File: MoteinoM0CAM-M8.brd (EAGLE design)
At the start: 22.6 x 22.2 mm, 17 parts

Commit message: doco update
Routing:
- net GND: vias 11 -> 12
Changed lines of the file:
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@@
 <via x="3.302" y="14.986" extent="1-16" drill="0.35"/>
 <via x="4.445" y="19.304" extent="1-16" drill="0.35"/>
+<via x="18.542" y="18.796" extent="1-16" drill="0.35"/>
+<wire x1="18.669" y1="16.129" x2="18.542" y2="18.796" width="0" layer="19" extent="1-1"/>
 </signal>
 <signal name="SDA">
@@
 <wire x1="7.112" y1="0" x2="7.088" y2="0" width="0.1524" layer="1"/>
 </signal>
-<signal name="N$13">
-<via x="18.542" y="18.796" extent="1-16" drill="0.35"/>
-</signal>
 </signals>

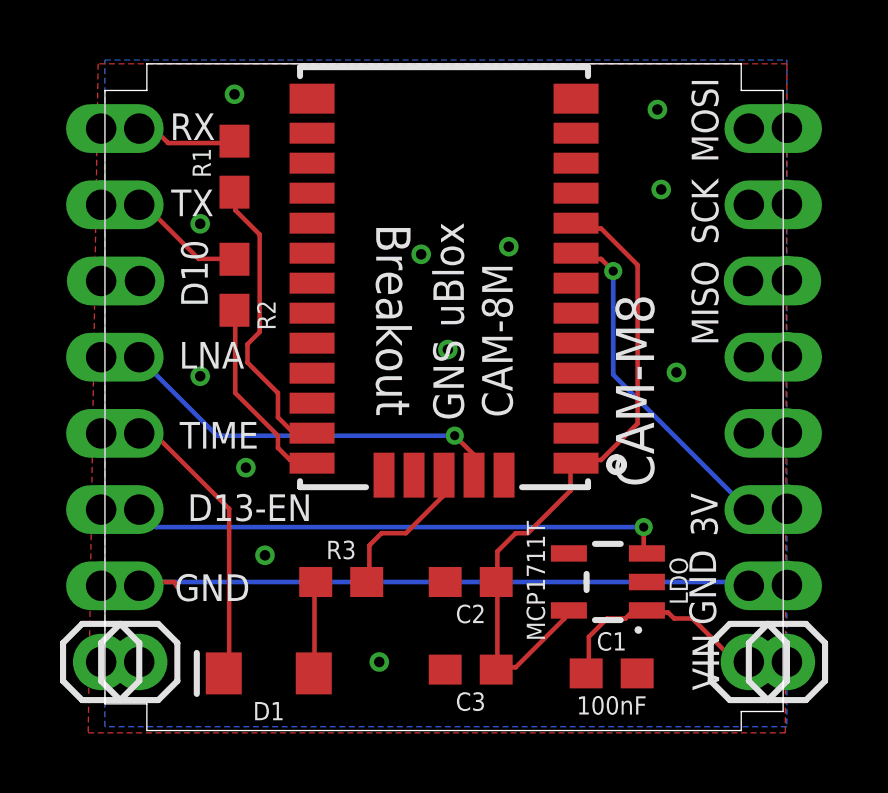
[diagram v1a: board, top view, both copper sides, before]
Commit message: Corrected 1203 to 0603 LED
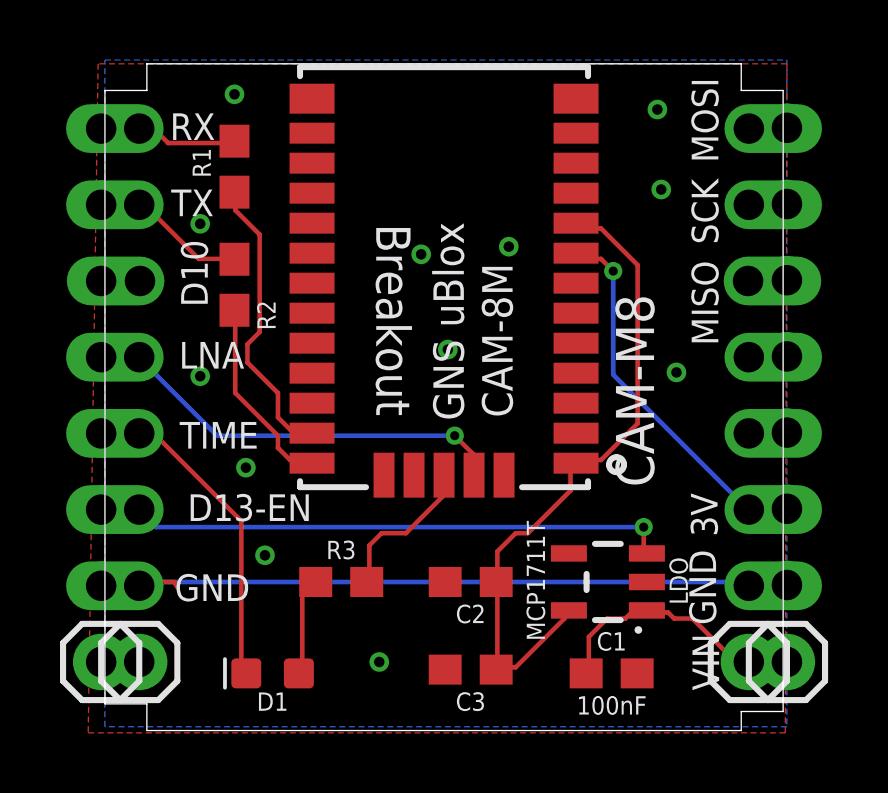
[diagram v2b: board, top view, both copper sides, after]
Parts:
- D1: device SparkFun-LED:LED-1206 -> SparkFun-LED:LED-0603
- moved D1 0.13 mm to (5.71, 0.00)
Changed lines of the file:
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@@
 <attribute name="VALUE" x="12.319" y="3.81" size="0.6096" layer="27" font="vector" ratio="20" rot="R180" align="top-center"/>
-</element>
-<element name="D1" library="SparkFun-LED" library_urn="urn:adsk.eagle:library:529" package="LED-1206" package3d_urn="urn:adsk.eagle:package:39352/1" value="GREEN" x="5.588" y="0" smashed="yes" rot="R180">
-<attribute name="NAME" x="5.588" y="-0.9525" size="0.6096" layer="25" font="vector" ratio="20" rot="R180" align="bottom-center"/>
-<attribute name="PROD_ID" value="DIO-00862" x="5.588" y="0" size="1.778" layer="27" rot="R180" display="off"/>
-<attribute name="VALUE" x="5.588" y="0.9525" size="0.6096" layer="27" font="vector" ratio="20" rot="R180" align="top-center"/>
 </element>
 <element name="R1" library="SparkFun-Resistors" library_urn="urn:adsk.eagle:library:532" package="0603" package3d_urn="urn:adsk.eagle:package:39650/1" value="220" x="4.445" y="16.891" smashed="yes" rot="R270">
@@
 <attribute name="PROD_ID" value="CAP-08280" x="12.319" y="0.127" size="1.778" layer="27" rot="R180" display="off"/>
 <attribute name="VALUE" x="12.319" y="0.889" size="0.6096" layer="27" font="vector" ratio="20" rot="R180" align="top-center"/>
+</element>
+<element name="D1" library="SparkFun-LED" library_urn="urn:adsk.eagle:library:529" package="LED-0603" package3d_urn="urn:adsk.eagle:package:39354/1" value="GREEN" x="5.715" y="0" smashed="yes" rot="R180">
+<attribute name="NAME" x="5.715" y="-0.635" size="0.6096" layer="25" font="vector" ratio="20" rot="R180" align="bottom-center"/>
+<attribute name="PROD_ID" value="DIO-00821" x="5.715" y="0" size="1.778" layer="27" rot="R180" display="off"/>
+<attribute name="VALUE" x="5.715" y="0.635" size="0.6096" layer="27" font="vector" ratio="20" rot="R180" align="top-center"/>
 </element>
 </elements>
@@
 <via x="4.445" y="19.304" extent="1-16" drill="0.35"/>
 <via x="18.542" y="18.796" extent="1-16" drill="0.35"/>
-<wire x1="18.669" y1="16.129" x2="18.542" y2="18.796" width="0" layer="19" extent="1-1"/>
 </signal>
 <signal name="SDA">
@@
 <signal name="D12_TIMEPULSE">
 <contactref element="U$17" pad="3"/>
+<wire x1="1.8288" y1="7.9248" x2="4.6736" y2="5.08" width="0.1524" layer="1"/>
+<wire x1="1.4224" y1="7.9248" x2="1.8288" y2="7.9248" width="0.1524" layer="1"/>
+<wire x1="1.4224" y1="7.9248" x2="1.27" y2="8.001" width="0.1524" layer="1"/>
 <contactref element="D1" pad="C"/>
-<wire x1="4.2672" y1="5.4864" x2="4.2672" y2="0" width="0.1524" layer="1"/>
-<wire x1="1.8288" y1="7.9248" x2="4.2672" y2="5.4864" width="0.1524" layer="1"/>
-<wire x1="1.4224" y1="7.9248" x2="1.8288" y2="7.9248" width="0.1524" layer="1"/>
-<wire x1="4.2672" y1="0" x2="4.088" y2="0" width="0.1524" layer="1"/>
-<wire x1="1.4224" y1="7.9248" x2="1.27" y2="8.001" width="0.1524" layer="1"/>
+<wire x1="4.6736" y1="5.08" x2="4.6736" y2="0" width="0.1524" layer="1"/>
+<wire x1="4.6736" y1="0" x2="4.838" y2="0" width="0.1524" layer="1"/>
 </signal>
 <signal name="D11_LNA_EN">
@@
 <contactref element="R3" pad="1"/>
 <contactref element="D1" pad="A"/>
-<wire x1="7.112" y1="0" x2="7.112" y2="3.048" width="0.1524" layer="1"/>
+<wire x1="6.7056" y1="2.6416" x2="6.7056" y2="0" width="0.1524" layer="1"/>
+<wire x1="7.112" y1="3.048" x2="6.7056" y2="2.6416" width="0.1524" layer="1"/>
+<wire x1="6.7056" y1="0" x2="6.592" y2="0" width="0.1524" layer="1"/>
 <wire x1="7.112" y1="3.048" x2="7.151" y2="3.048" width="0.1524" layer="1"/>
-<wire x1="7.112" y1="0" x2="7.088" y2="0" width="0.1524" layer="1"/>
 </signal>
 </signals>
